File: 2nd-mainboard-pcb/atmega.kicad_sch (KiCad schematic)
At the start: 16 parts, among them U10 ATmega328PB-A, Y1 ECS-160-18-4X-CKM

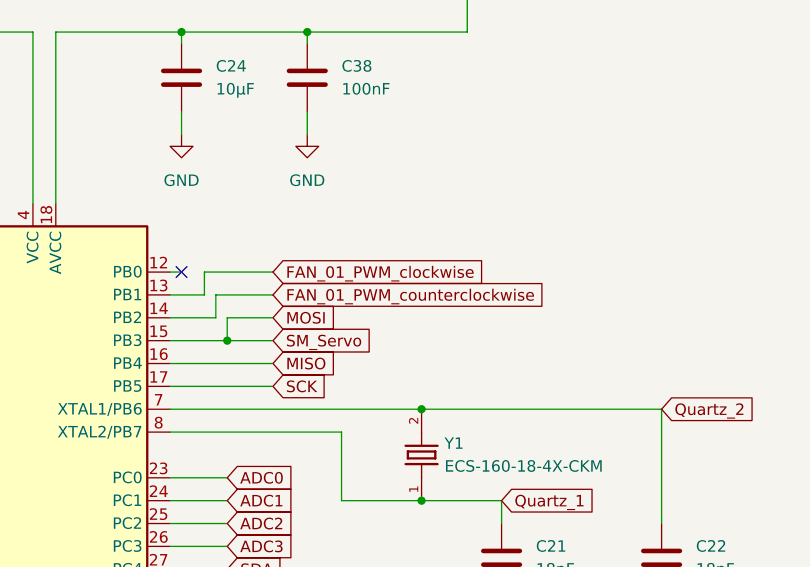
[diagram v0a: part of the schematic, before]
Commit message: made better connections
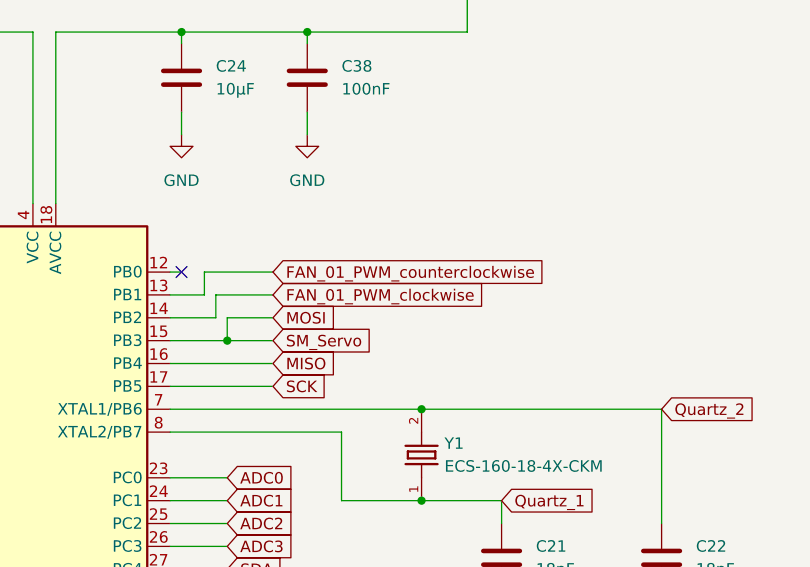
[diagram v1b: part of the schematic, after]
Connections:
- net FAN_01_PWM_clockwise: now also U10.14 (PB2); no longer U10.13 (PB1)
- net FAN_01_PWM_counterclockwise: now also U10.13 (PB1); no longer U10.14 (PB2)

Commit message: last few changes
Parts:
- added R18: 0, Resistor_SMD:R_0603_1608Metric_Pad0.98x0.95mm_HandSolder, symbol Device:R
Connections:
- net RESET: now also R18.2; no longer U10.29 (~{RESET}/PC6)
- new net: R18.1, U10.29 (~{RESET}/PC6)
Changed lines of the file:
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@@
 	(wire
 		(pts
+			(xy 104.14 101.6) (xy 109.22 101.6)
+		)
+		(stroke
+			(width 0)
+			(type default)
+		)
+	)
+	(wire
+		(pts
 			(xy 198.12 74.93) (xy 198.12 73.66)
 		)
@@
 	(wire
 		(pts
-			(xy 92.71 101.6) (xy 99.06 101.6)
+			(xy 92.71 101.6) (xy 96.52 101.6)
 		)
 		(stroke
@@
 	(global_label "RESET"
 		(shape input)
-		(at 99.06 101.6 0)
+		(at 109.22 101.6 0)
 		(fields_autoplaced yes)
 		(effects
@@
 		)
 		(property "Intersheetrefs" "${INTERSHEET_REFS}"
-			(at 107.7903 101.6 0)
+			(at 117.9503 101.6 0)
 			(effects
 				(font
@@
 					(unit 1)
 				)
+			)
+		)
+	)
+	(symbol
+		(lib_id "Device:R")
+		(at 100.33 101.6 90)
+		(unit 1)
+		(exclude_from_sim no)
+		(in_bom yes)
+		(on_board yes)
+		(dnp no)
+		(property "Reference" "R18"
+			(at 98.552 103.632 90)
+			(effects
+				(font
+					(size 1.27 1.27)
+				)
+			)
+		)
+		(property "Value" "0"
+			(at 101.854 103.632 90)
+			(effects
+				(font
+					(size 1.27 1.27)
+				)
+			)
+		)
+		(property "Footprint" "Resistor_SMD:R_0603_1608Metric_Pad0.98x0.95mm_HandSolder"
+			(at 100.33 103.378 90)
+			(effects
+				(font
+					(size 1.27 1.27)
+				)
+				(hide yes)
+			)
+		)
+		(property "Datasheet" "~"
+			(at 100.33 101.6 0)
+			(effects
+				(font
+					(size 1.27 1.27)
+				)
+				(hide yes)
+			)
+		)
+		(property "Description" "Resistor"
+			(at 100.33 101.6 0)
+			(effects
+				(font
+					(size 1.27 1.27)
+				)
+				(hide yes)
+			)
+		)
+		(pin "1"
+		)
+		(pin "2"
+		)
+		(instances
+			(project ""
+				(path "/6926a609-8b92-4b3a-88c8-3d023174b977/2814f85c-0b7e-4ab3-b3e5-bcf29424baab"
+					(reference "R18")
+					(unit 1)
+				)
